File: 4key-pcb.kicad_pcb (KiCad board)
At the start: 2 copper layers, 82.6 x 38.1 mm, 25 parts

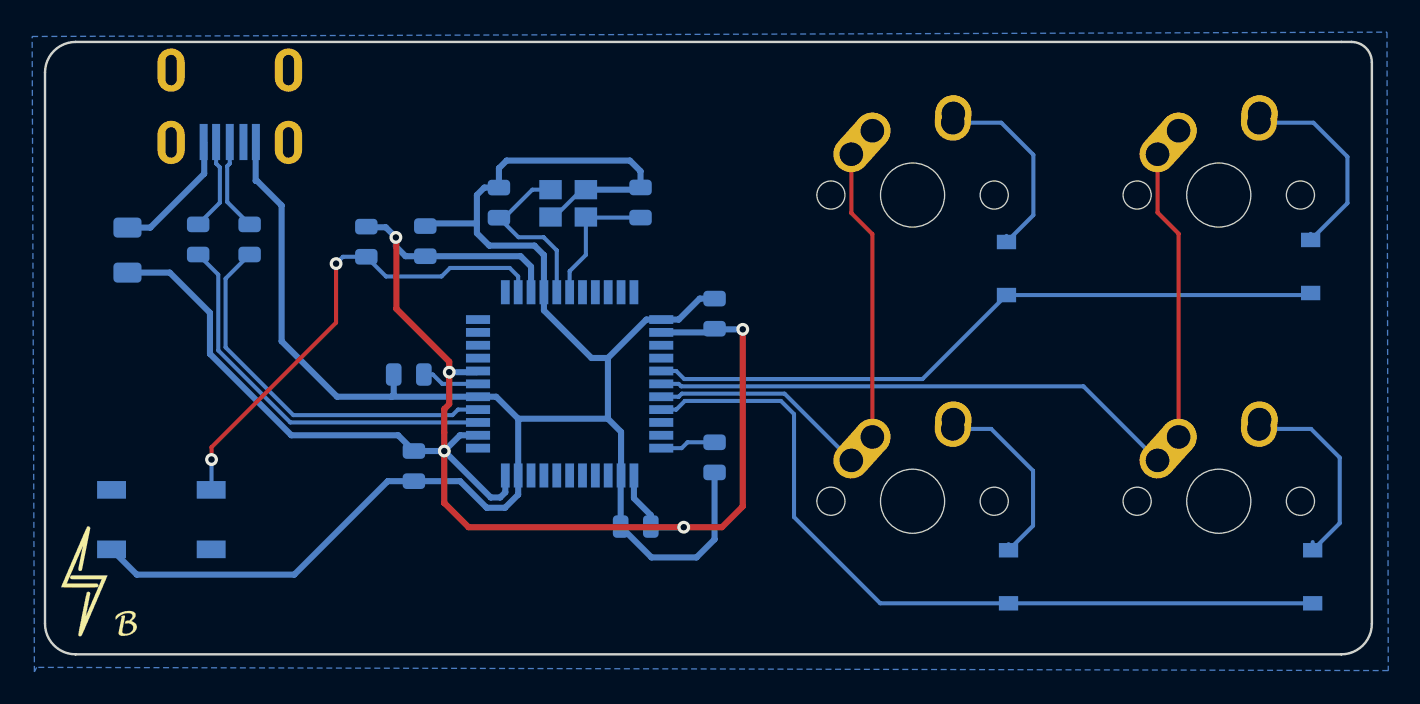
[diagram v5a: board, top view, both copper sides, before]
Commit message: updated to usb-c
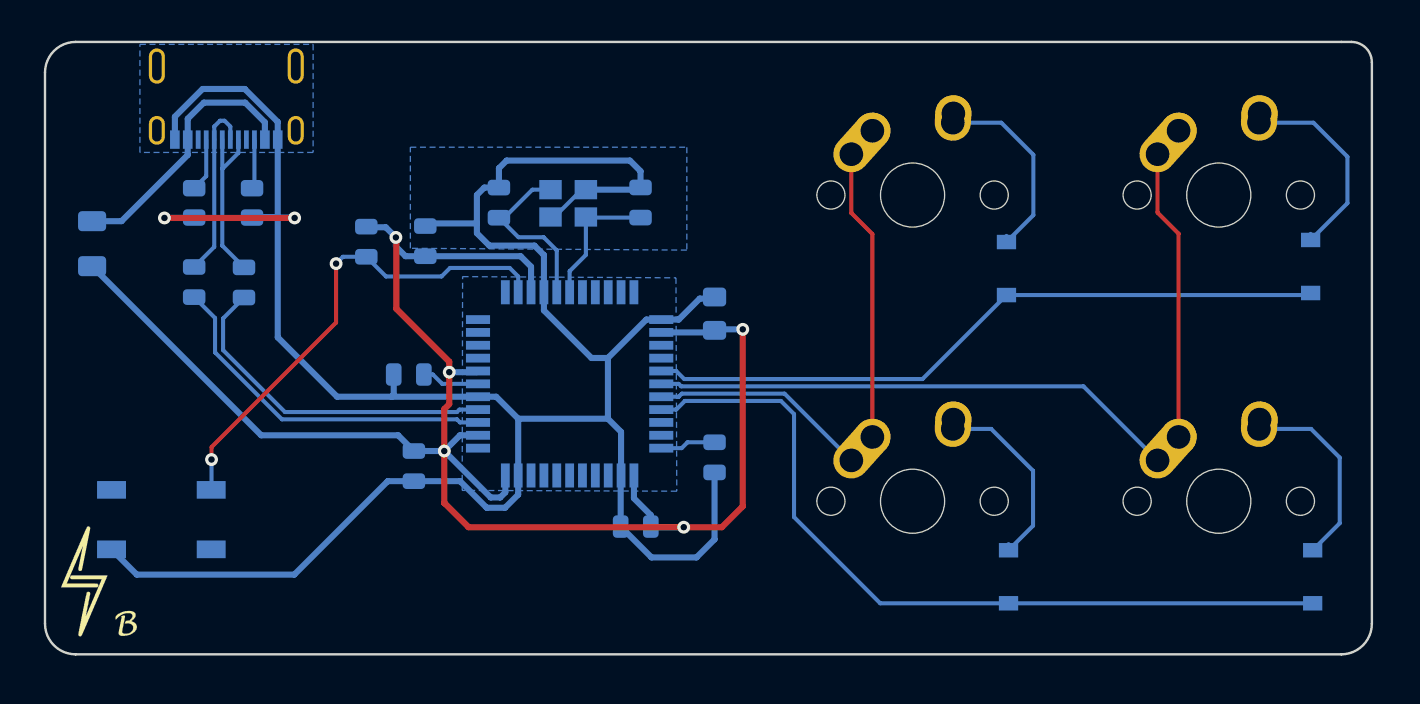
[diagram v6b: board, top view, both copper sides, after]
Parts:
- removed R-D-1: 22, Resistor_SMD:R_0805_2012Metric
- added RCC1: 5.1K, Resistor_SMD:R_0805_2012Metric, B.Cu at (61.4, 97.3)
- added RCC2: 5.1K, Resistor_SMD:R_0805_2012Metric, B.Cu at (65.0, 97.3)
- added RD-1: 22, Resistor_SMD:R_0805_2012Metric, B.Cu at (61.4, 102.2)
- C1: footprint Capacitor_SMD:C_0805_2012Metric -> Capacitor_SMD:C_0805_2012Metric_Pad1.18x1.45mm_HandSolder
- USB1: value Molex-0548190589 -> Molex_USB_C_2171790001; footprint random-keyboard-parts:Molex-0548190589 -> Connector_Molex:Molex_USB-C_2171790001
- moved RD+1 2.70 mm to (64.5, 102.2)
- moved F-USB1 2.24 mm to (55.0, 99.8)
- moved USB1 0.86 mm to (63.4, 90.8), turned to 0 degrees
- renumbered R-D+1 to RD+1
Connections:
- USB1 pad 2: Net-(USB1-Pad2) -> VCC
- USB1 pad 3: D+ -> Net-(USB1-Pad3)
- USB1 pad 4: D- -> Net-(RCC1-Pad1)
- USB1 pad 5: VCC -> D-
- USB1 pad 6: Net-(USB1-Pad6) -> D+
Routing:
- net GND: track 139.6 -> 163.9 mm, vias 0 -> 2
- net VCC: track 8.15 -> 16.7 mm
- net D-: track 5.78 -> 11.4 mm
- net D+: track 5.77 -> 10.7 mm
- net Net-(RCC1-Pad1): track 0.00 -> 3.34 mm
- net Net-(RCC2-Pad1): track 0.00 -> 3.09 mm
- net Net-(MCU1-Pad4): track 24.0 -> 21.3 mm
- net Net-(MCU1-Pad3): track 24.5 -> 22.1 mm
- net +5V: track 109.2 -> 110.0 mm
- net Net-(D4-Pad2): track 12.7 -> 12.2 mm
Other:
- rule pad_to_mask_clearance: 0.051 -> 0
